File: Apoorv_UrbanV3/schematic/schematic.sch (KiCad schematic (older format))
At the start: 15 parts

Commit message: ALMOST DONE, ROUTING LEFT
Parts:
- removed TRANSCEIVER1: MCP2561-THROUGH, schematic:DIP787W46P254L927H533Q8, symbol schematic-eagle-import:MCP2561-THROUGH
- added H1, H2, H3, H4: MountingHole_Pad, MountingHole:MountingHole_5mm_Pad, symbol Mechanical:MountingHole_Pad
- added S2: DS04-254-2-01BK-SMT, SW_DS04-254-2-01BK-SMT, symbol DS04-254-2-01BK-SMT:DS04-254-2-01BK-SMT
- added U1: MCP2561T-E_MF, MCP2561:MCP2561T-E&slash_MF, symbol 2020-11-27_17-21-33:MCP2561T-E_MF
- DMS1: footprint eec:Molex-15-91-2045-0-0-0 -> 15-91-2035:15912035
- R1, R2, R3_DNP1: footprint schematic:0207_10 -> 10k_resistor:RESC1608X55N
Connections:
- wire segments 106 -> 121
- no-connect marks 13 -> 14
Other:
- moved on the sheet: R3_DNP1
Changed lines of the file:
@@
 +5V
-Wire Wire Line
-	1500 3500 1000 3500
 Wire Wire Line
 	1000 3500 1000 3400
@@
 GND
 Wire Wire Line
-	2500 3300 2700 3300
-Wire Wire Line
 	2700 3300 2700 3700
 Text Label 2500 3300 0    10   ~ 0
 GND
 Wire Wire Line
-	1500 3400 1200 3400
-Wire Wire Line
 	1200 3400 1200 3700
 Text Label 1500 3400 0    10   ~ 0
@@
 	4900 5900 4900 5100
 Wire Wire Line
-	4900 5100 6800 5100
-Wire Wire Line
 	7400 5100 7400 4000
 Wire Wire Line
@@
 Wire Wire Line
 	4100 6000 4100 5000
-Wire Wire Line
-	4100 5000 7300 5000
 Wire Wire Line
 	7300 5000 7300 4100
@@
 	3700 4400 5100 4400
 Wire Wire Line
-	2500 3400 2900 3400
-Wire Wire Line
 	5400 1900 2900 1900
-Wire Wire Line
-	2900 1900 2900 3200
-Wire Wire Line
-	2900 3200 2900 3400
-Connection ~ 2900 3200
 Wire Wire Line
 	4100 2500 4100 4100
@@
 F 0 "R1" H 4550 5959 59  0000 L BNN
 F 1 "100K" H 4650 5770 59  0000 L BNN
-F 2 "schematic:0207_10" H 4700 5900 50  0001 C CNN
+F 2 "10k_resistor:RESC1608X55N" H 4700 5900 50  0001 C CNN
 F 3 "" H 4700 5900 50  0001 C CNN
 	1    4700 5900
@@
 F 0 "R2" H 5050 6359 59  0000 L BNN
 F 1 "100" H 5050 6170 59  0000 L BNN
-F 2 "schematic:0207_10" H 5200 6300 50  0001 C CNN
+F 2 "10k_resistor:RESC1608X55N" H 5200 6300 50  0001 C CNN
 F 3 "" H 5200 6300 50  0001 C CNN
 	1    5200 6300
-	1    0    0    -1
-$EndComp
-$Comp
-L schematic-eagle-import:MCP2561-THROUGH TRANSCEIVER1
-U 1 1 CC846E78
-P 2000 3500
-F 0 "TRANSCEIVER1" H 1700 3800 59  0000 L BNN
-F 1 "MCP2561-THROUGH" H 2000 3500 50  0001 C CNN
-F 2 "schematic:DIP787W46P254L927H533Q8" H 2000 3500 50  0001 C CNN
-F 3 "" H 2000 3500 50  0001 C CNN
-	1    2000 3500
 	1    0    0    -1
 $EndComp
@@
 L schematic-eagle-import:R-US_0207_10 R3_DNP1
 U 1 1 93EDAD52
-P 3100 3200
-F 0 "R3_DNP1" H 2950 3259 59  0000 L BNN
-F 1 "120" H 3050 3070 59  0000 L BNN
-F 2 "schematic:0207_10" H 3100 3200 50  0001 C CNN
-F 3 "" H 3100 3200 50  0001 C CNN
-	1    3100 3200
+P 3100 3350
+F 0 "R3_DNP1" H 2850 3450 59  0000 L BNN
+F 1 "120" H 3050 3220 59  0000 L BNN
+F 2 "10k_resistor:RESC1608X55N" H 3100 3350 50  0001 C CNN
+F 3 "" H 3100 3350 50  0001 C CNN
+	1    3100 3350
 	1    0    0    -1
 $EndComp
@@
 	0    1    1    0
 $EndComp
-Wire Wire Line
-	2500 3500 3700 3500
 Wire Wire Line
 	3700 2000 5600 2000
@@
 	-1   0    0    1
 $EndComp
-Wire Wire Line
-	6800 5100 6800 3600
 $Comp
 L eec:MOLEX-15-91-2035-PIN_HEADER DMS1
@@
 F 0 "DMS1" V 7000 4800 50  0000 R CNN
 F 1 "MOLEX-15-91-2035-PIN_HEADER" V 6700 5850 50  0000 R CNN
-F 2 "eec:Molex-15-91-2045-0-0-0" H 6900 5700 50  0001 C CNN
+F 2 "15-91-2035:15912035" H 6900 5700 50  0001 C CNN
 F 3 "" H 6900 5700 50  0001 C CNN
 	1    7000 5750
@@
 Wire Wire Line
 	7900 4300 8750 4300
-Connection ~ 6800 3600
-Connection ~ 6800 5100
-Wire Wire Line
-	6800 5100 7400 5100
 NoConn ~ 7500 2100
 Wire Wire Line
@@
 	3700 6000 2000 6000
 Wire Wire Line
-	3700 2000 3700 3200
-Wire Wire Line
-	3300 3200 3700 3200
-Connection ~ 3700 3200
-Wire Wire Line
-	3700 3200 3700 3500
+	4900 5100 7400 5100
+Wire Wire Line
+	6800 3600 6800 5000
+Wire Wire Line
+	4100 5000 6800 5000
+Connection ~ 6800 3600
+Connection ~ 6800 5000
+Wire Wire Line
+	6800 5000 7300 5000
+Wire Wire Line
+	3700 2000 3700 3050
+Connection ~ 2900 3350
+Wire Wire Line
+	2900 3350 2900 3400
+Wire Wire Line
+	2900 1900 2900 3350
+$Comp
+L DS04-254-2-01BK-SMT:DS04-254-2-01BK-SMT S2
+U 1 1 5FC31F31
+P 3500 3050
+F 0 "S2" H 3500 3299 50  0000 C CNN
+F 1 "DS04-254-2-01BK-SMT" H 3500 3208 50  0000 C CNN
+F 2 "SW_DS04-254-2-01BK-SMT" H 3750 3300 50  0001 L BNN
+F 3 "" H 3500 3050 50  0001 L BNN
+F 4 "Manufacturer Recommendations" H 3700 3200 50  0001 L BNN "STANDARD"
+F 5 "CUI Inc." H 3450 3400 50  0001 L BNN "MANUFACTURER"
+F 6 "V0.0" H 3500 3050 50  0001 L BNN "PARTREV"
+F 7 "4.86 mm" H 3500 3300 50  0001 L BNN "MAXIMUM_PACKAGE_HEIGHT"
+	1    3500 3050
+	1    0    0    -1
+$EndComp
+Connection ~ 3700 3050
+Wire Wire Line
+	3700 3050 3700 3500
+Wire Wire Line
+	3300 3050 3300 3350
+$Comp
+L 2020-11-27_17-21-33:MCP2561T-E_MF U1
+U 1 1 5FC18B7D
+P 850 3350
+F 0 "U1" H 1975 3657 60  0000 C CNN
+F 1 "MCP2561T-E_MF" H 1975 3551 60  0000 C CNN
+F 2 "MCP2561:MCP2561T-E&slash_MF" H 2050 3590 60  0001 C CNN
+F 3 "" H 850 3350 60  0000 C CNN
+	1    850  3350
+	1    0    0    -1
+$EndComp
+Wire Wire Line
+	2450 3500 2450 3600
+Wire Wire Line
+	2450 3600 2300 3600
+Wire Wire Line
+	2450 3500 3700 3500
+Wire Wire Line
+	2400 3400 2400 3500
+Wire Wire Line
+	2400 3500 2300 3500
+Wire Wire Line
+	2400 3400 2900 3400
+Wire Wire Line
+	2300 3300 2350 3300
+Wire Wire Line
+	2350 3300 2350 3400
+Wire Wire Line
+	2350 3400 2300 3400
+Connection ~ 2350 3300
+Wire Wire Line
+	2350 3300 2700 3300
+Wire Wire Line
+	1500 3600 1650 3600
+Wire Wire Line
+	1000 3500 1650 3500
+Wire Wire Line
+	1200 3400 1650 3400
+Wire Wire Line
+	1500 3300 1650 3300
+NoConn ~ 2300 3700
+$Comp
+L Mechanical:MountingHole_Pad H2
+U 1 1 5FC61EAF
+P 8950 5700
+F 0 "H2" H 9050 5749 50  0000 L CNN
+F 1 "MountingHole_Pad" H 9050 5658 50  0000 L CNN
+F 2 "MountingHole:MountingHole_5mm_Pad" H 8950 5700 50  0001 C CNN
+F 3 "~" H 8950 5700 50  0001 C CNN
+	1    8950 5700
+	1    0    0    -1
+$EndComp
+$Comp
+L Mechanical:MountingHole_Pad H3
+U 1 1 5FC638AF
+P 9200 5950
+F 0 "H3" H 9300 5999 50  0000 L CNN
+F 1 "MountingHole_Pad" H 9300 5908 50  0000 L CNN
+F 2 "MountingHole:MountingHole_5mm_Pad" H 9200 5950 50  0001 C CNN
+F 3 "~" H 9200 5950 50  0001 C CNN
+	1    9200 5950
+	1    0    0    -1
+$EndComp
+$Comp
+L Mechanical:MountingHole_Pad H4
+U 1 1 5FC63F31
+P 9400 6200
+F 0 "H4" H 9500 6249 50  0000 L CNN
+F 1 "MountingHole_Pad" H 9500 6158 50  0000 L CNN
+F 2 "MountingHole:MountingHole_5mm_Pad" H 9400 6200 50  0001 C CNN
+F 3 "~" H 9400 6200 50  0001 C CNN
+	1    9400 6200
+	1    0    0    -1
+$EndComp
+$Comp
+L Mechanical:MountingHole_Pad H1
+U 1 1 5FC64392
+P 8800 5450
+F 0 "H1" H 8900 5499 50  0000 L CNN
+F 1 "MountingHole_Pad" H 8900 5408 50  0000 L CNN
+F 2 "MountingHole:MountingHole_5mm_Pad" H 8800 5450 50  0001 C CNN
+F 3 "~" H 8800 5450 50  0001 C CNN
+	1    8800 5450
+	1    0    0    -1
+$EndComp
+Wire Wire Line
+	8800 5550 8800 5800
+Wire Wire Line
+	8800 5800 8950 5800
+Wire Wire Line
+	9200 6050 8950 6050
+Wire Wire Line
+	8950 6050 8950 5800
+Connection ~ 8950 5800
+Wire Wire Line
+	9400 6300 9200 6300
+Wire Wire Line
+	9200 6300 9200 6050
+Connection ~ 9200 6050
+$Comp
+L power:GND #PWR0102
+U 1 1 5FC71BB6
+P 8950 6050
+F 0 "#PWR0102" H 8950 5800 50  0001 C CNN
+F 1 "GND" H 8955 5877 50  0000 C CNN
+F 2 "" H 8950 6050 50  0001 C CNN
+F 3 "" H 8950 6050 50  0001 C CNN
+	1    8950 6050
+	1    0    0    -1
+$EndComp
+Connection ~ 8950 6050
 $EndSCHEMATC

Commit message: V3 done design review pending
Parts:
- removed U1: MCP2561T-E_MF, MCP2561:MCP2561T-E&slash_MF, symbol 2020-11-27_17-21-33:MCP2561T-E_MF
- added 3V3, 5V1, CAN_H1, CAN_L1, GND1: TestPoint, TestPoint:TestPoint_THTPad_D4.0mm_Drill2.0mm, symbol Connector:TestPoint
- added CAN_TRNSVR1: `, footprints:MCP2562FD-H&slash_P, symbol 2020-11-28_19-28-36:MCP2562FD-H_P
- added H5, H6, H7, H8: MountingHole_Pad, MountingHole:MountingHole_3.2mm_M3_Pad, symbol Mechanical:MountingHole_Pad
- BRAKE+THROTTLE1: value MOLEX-15-91-2045-PIN_HEADER -> `
- DMS1: value MOLEX-15-91-2035-PIN_HEADER -> `
- H1, H2, H3, H4: footprint MountingHole:MountingHole_5mm_Pad -> MountingHole:MountingHole_3.2mm_M3_Pad
- HAZARDS1, IGNITION1, LIGHTS1, WIPERS1: value LP11EE1NCSYG -> `
- HORN1: value LP11OA1TCSYY -> `
- INDICATORS1: renamed from S1; value M2013TXG13-DA -> `
- S_CAN1: renamed from S2; value DS04-254-2-01BK-SMT -> ~
- renumbered 2.2TFT1 to LCD1, R3_DNP1 to R_CAN1
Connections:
- net +3V3: now also HAZARDS1.1, IGNITION1.1, INDICATORS1.2 (COM), LIGHTS1.1, WIPERS1.1, 3V3.1, CAN_TRNSVR1.5 (VIO); no longer LCD1.1 (3V3), R2.1, STM32L432.17 (3V3)
- net GND: now also INDICATORS1.SH1 (SH), INDICATORS1.SH2 (SH), INDICATORS1.SH3 (SH), INDICATORS1.SH4 (SH), STM32L432.4 (GND1), CAN_TRNSVR1.2 (VSS), CAN_TRNSVR1.8 (STBY), GND1.1, H5.1, H6.1, H7.1, H8.1; no longer LCD1.2 (GND)
- net LCD_LED: now reaches LCD1.8 (LED), R2.2
- net IGNITION: now reaches IGNITION1.2, STM32L432.9 (D6)
- net CAN_L: now reaches MAINPLUG1.2, S_CAN1.1B
- net CAN_L: now also CAN_L1.1, CAN_TRNSVR1.6 (CANL)
- net CAN_H: now reaches MAINPLUG1.3, R_CAN1.1
- net CAN_H: now also CAN_H1.1, CAN_TRNSVR1.7 (CANH)
- net WIPRERS: now reaches STM32L432.21 (A2), WIPERS1.2
- net LIGHTS: now reaches LIGHTS1.2, STM32L432.19 (A0)
- net HAZARDS: now reaches HAZARDS1.2, STM32L432.12 (D9)
- net HORN: now reaches HORN1.2, STM32L432.8 (D5)
- net DMS: now reaches DMS1.2, STM32L432.20 (A1)
- net IND_LEFT: now reaches INDICATORS1.LEFT, STM32L432.7 (D4)
- net IND_RIGHT: now reaches INDICATORS1.RIGHT, STM32L432.6 (D3)
- net TXD: now reaches STM32L432.5 (D2)
- net TXD: now also CAN_TRNSVR1.1 (TXD)
- net RXD: now reaches STM32L432.13 (D10)
- net RXD: now also CAN_TRNSVR1.4 (RXD)
- net LCD_RST: now reaches LCD1.4 (RST), R1.2, STM32L432.23 (A4)
- net LCD_CS: now reaches LCD1.3 (CS), STM32L432.24 (A5)
- net LCD_MOSI: now reaches LCD1.6 (MOSI), STM32L432.14 (D11)
- net LCD_SCK: now reaches LCD1.7 (SCK), STM32L432.16 (D13)
- net LCD_MISO: now reaches LCD1.9 (MISO), STM32L432.15 (D12)
- net +5V renamed LCD_DC
- no-connect marks 14 -> 22
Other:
- moved on the sheet: BRAKE+THROTTLE1, DMS1, H1, H2, H3, H4, HAZARDS1, HORN1, IGNITION1, INDICATORS1, LCD1, LIGHTS1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

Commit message: EVERYTHING COMPLETE POST DESIGN REVIEW
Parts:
- added DMS2: TestPoint, TestPoint:TestPoint_THTPad_D4.0mm_Drill2.0mm, symbol Connector:TestPoint
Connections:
- net LCD_DC is gone; now on net 5V: LCD1.5 (DC), STM32L432.22 (A3), STM32L432.27 (5V)
- net DMS: now also DMS2.1
- net LCD_CS: now also STM32L432.26 (A7); no longer STM32L432.24 (A5)
- net LCD_RST: now also STM32L432.2 (D0); no longer STM32L432.23 (A4)
- net 5V: now reaches 5V1.1

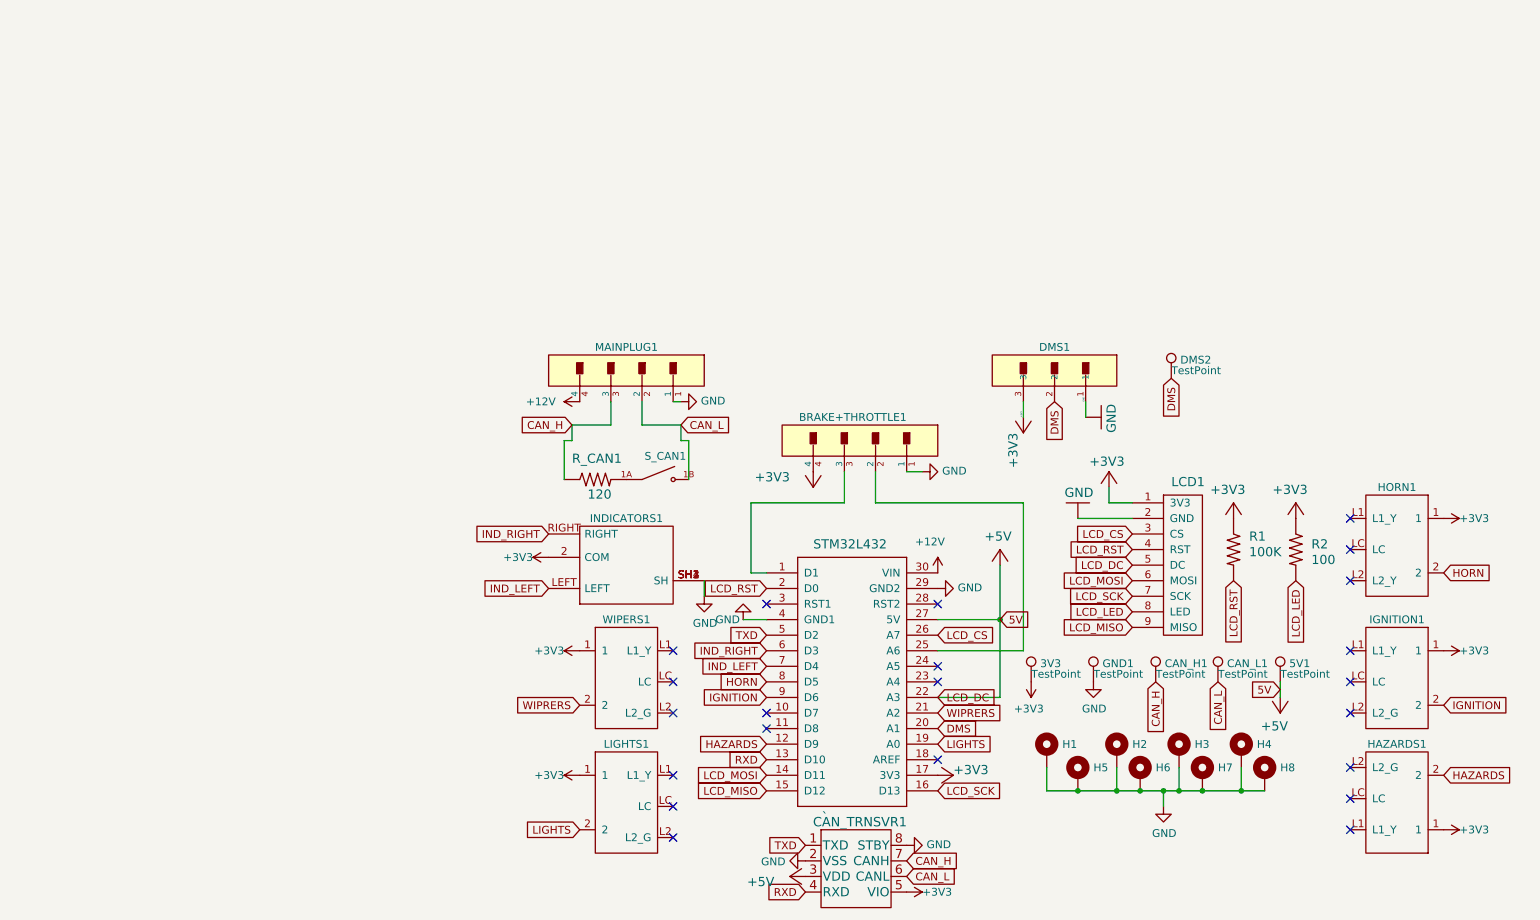
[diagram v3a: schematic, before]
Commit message: Cleaned up labels and fixed DRC warnings
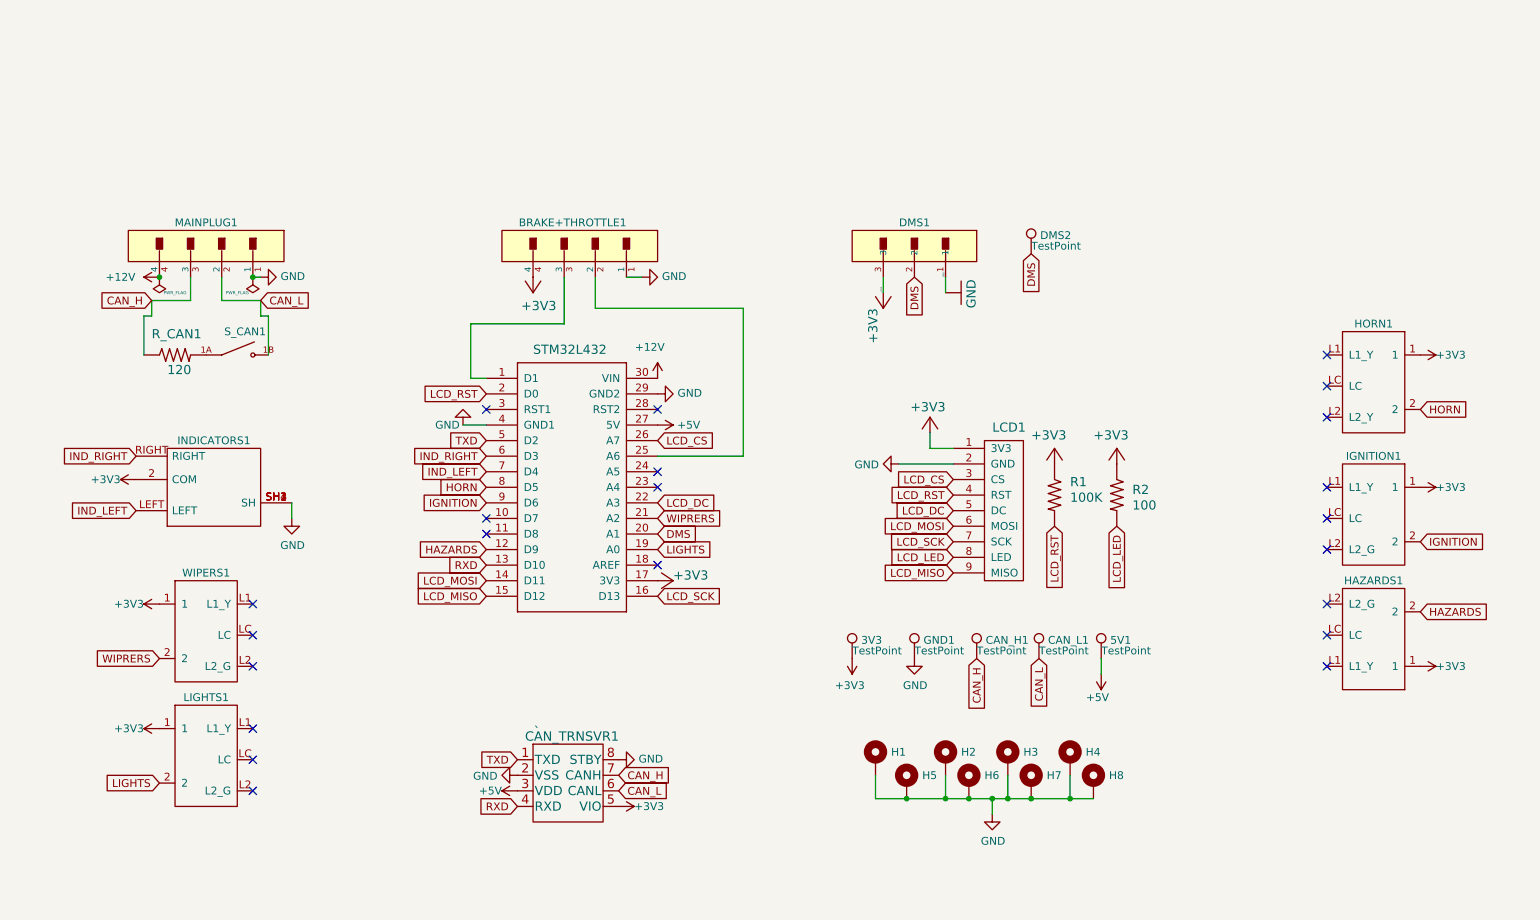
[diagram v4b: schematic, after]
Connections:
- net GND: now also LCD1.2 (GND)
- net +5V: now reaches CAN_TRNSVR1.3 (VDD)
- net +5V: now also 5V1.1, STM32L432.27 (5V)
- net 5V renamed LCD_DC
- net LCD_DC: no longer 5V1.1, STM32L432.27 (5V)
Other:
- moved on the sheet: 3V3, 5V1, BRAKE+THROTTLE1, CAN_H1, CAN_L1, CAN_TRNSVR1, DMS1, DMS2, GND1, H1, H2, H3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
